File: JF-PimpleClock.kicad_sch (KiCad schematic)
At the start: 59 parts, among them J1 Conn_01x06_Female, J2 Conn_01x02, J3 Conn_01x02, J4 USB_B_Micro, Q1 Q_PMOS_DSG, SW1 SW_Push, SW2 SW_Push, SW3 SW_Push, SW4 SW_Push, U1 ATmega328-P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

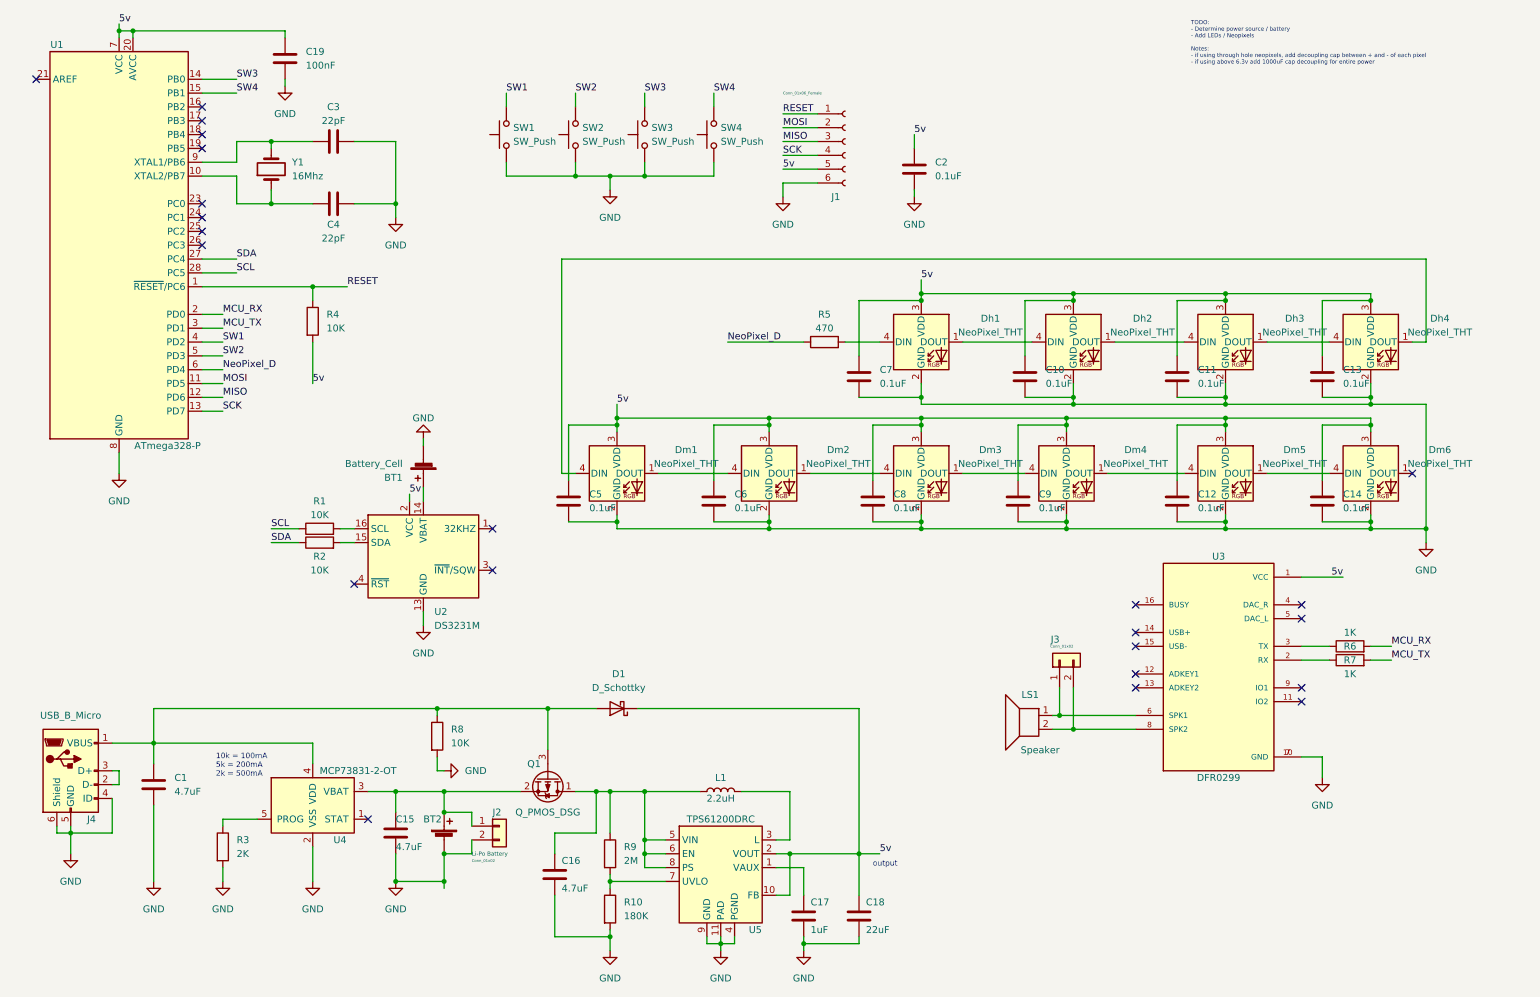
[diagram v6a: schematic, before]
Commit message: revision 2, changed some parts for making it easier to manufacture, fixed the issue with the wrong atmega footprint, added more test points
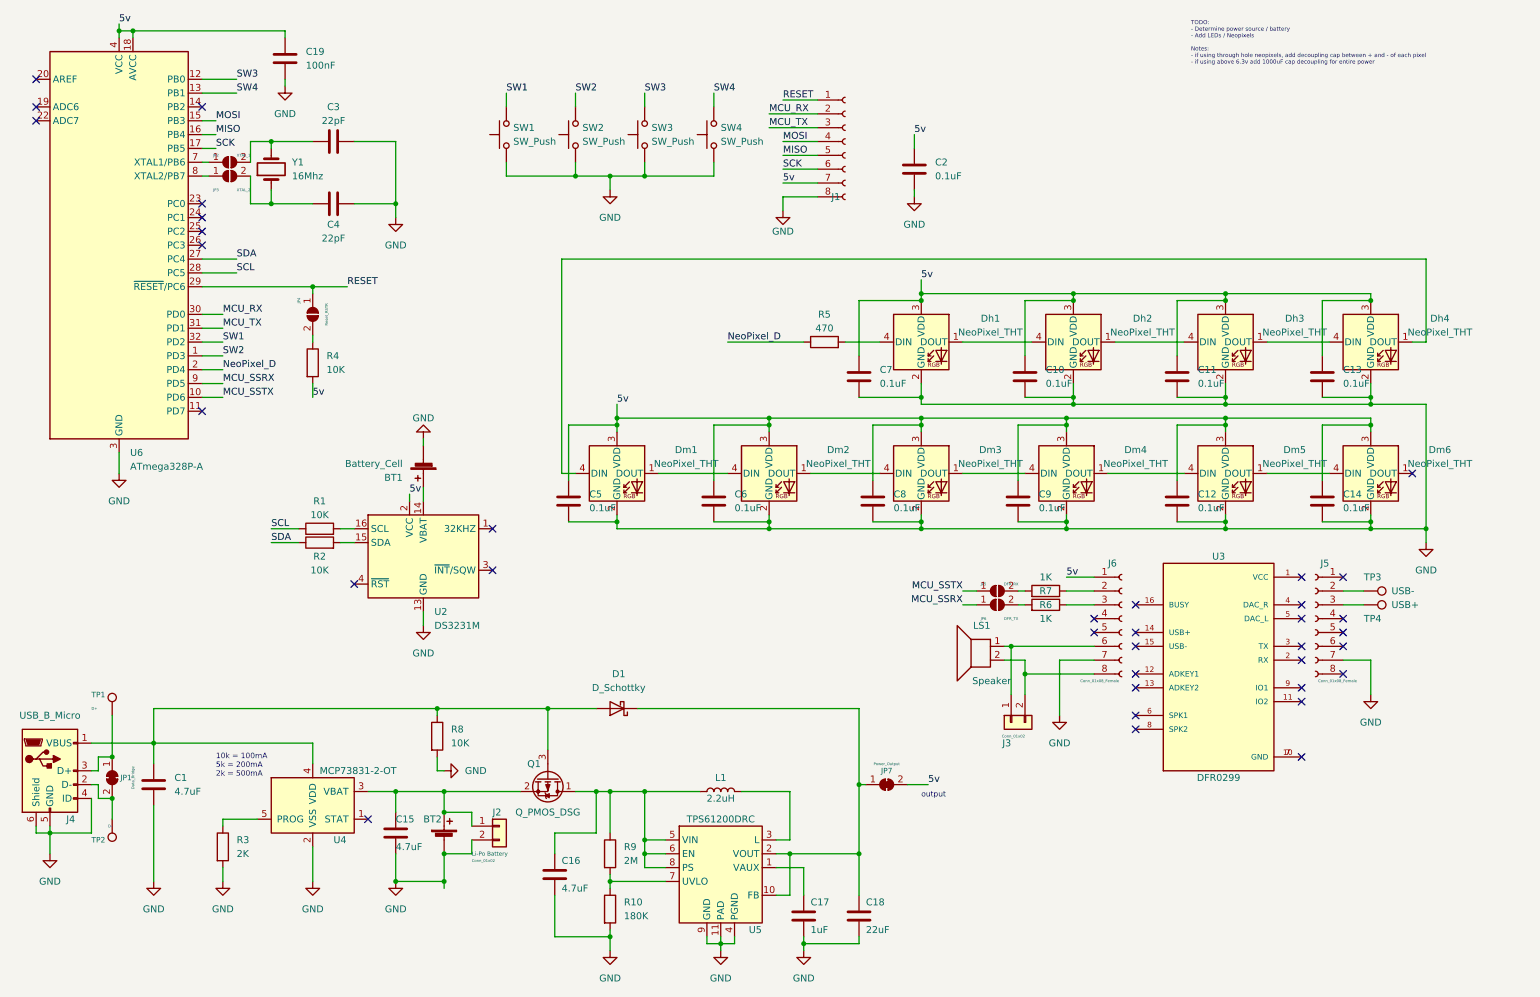
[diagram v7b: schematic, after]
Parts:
- removed U1: ATmega328-P, Package_QFP:TQFP-32_7x7mm_P0.8mm, symbol MCU_Microchip_ATmega:ATmega328-P
- added J5, J6: Conn_01x08_Female, Connector_PinHeader_2.54mm:PinHeader_1x08_P2.54mm_Vertical, symbol Connector:Conn_01x08_Female
- added JP1: Data_Bridge, Jumper:SolderJumper-2_P1.3mm_Bridged_Pad1.0x1.5mm, symbol Jumper:SolderJumper_2_Bridged
- added JP2: XTAL_1, Jumper:SolderJumper-2_P1.3mm_Open_Pad1.0x1.5mm, symbol Jumper:SolderJumper_2_Open
- added JP3: XTAL_2, Jumper:SolderJumper-2_P1.3mm_Open_Pad1.0x1.5mm, symbol Jumper:SolderJumper_2_Open
- added JP4: Reset_RSTR, Jumper:SolderJumper-2_P1.3mm_Open_Pad1.0x1.5mm, symbol Jumper:SolderJumper_2_Open
- added JP5: DFR_RX, Jumper:SolderJumper-2_P1.3mm_Open_Pad1.0x1.5mm, symbol Jumper:SolderJumper_2_Open
- added JP6: DFR_TX, Jumper:SolderJumper-2_P1.3mm_Open_Pad1.0x1.5mm, symbol Jumper:SolderJumper_2_Open
- added JP7: Power_Output, Jumper:SolderJumper-2_P1.3mm_Bridged_Pad1.0x1.5mm, symbol Jumper:SolderJumper_2_Bridged
- added TP1: D+, TestPoint:TestPoint_THTPad_2.5x2.5mm_Drill1.2mm, symbol Connector:TestPoint
- added TP2: D-, TestPoint:TestPoint_THTPad_2.5x2.5mm_Drill1.2mm, symbol Connector:TestPoint
- added TP3: USB-, TestPoint:TestPoint_THTPad_2.5x2.5mm_Drill1.2mm, symbol Connector:TestPoint
- added TP4: USB+, TestPoint:TestPoint_THTPad_2.5x2.5mm_Drill1.2mm, symbol Connector:TestPoint
- added U6: ATmega328P-A, Package_QFP:TQFP-32_7x7mm_P0.8mm, symbol MCU_Microchip_ATmega:ATmega328P-A
- J1: value Conn_01x06_Female -> Conn_01x08_Female; footprint Connector_PinHeader_2.54mm:PinHeader_1x06_P2.54mm_Vertical -> Connector_PinHeader_2.54mm:PinHeader_1x08_P2.54mm_Vertical; symbol Connector:Conn_01x06_Female -> Connector:Conn_01x08_Female
- SW1, SW2, SW3, SW4: footprint Button_Switch_SMD:SW_SPST_B3S-1100 -> Button_Switch_THT:SW_PUSH_6mm_H5mm
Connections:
- net 5v: now also J1.7 (Pin_7), J6.1 (Pin_1), JP7.2 (B), U6.18 (AVCC), U6.4 (VCC), U6.6 (VCC); no longer C18.1, D1.1 (K), J1.5 (Pin_5), U3.1 (VCC), U5.10 (FB), U5.2 (VOUT)
- net GND: now also J1.8 (Pin_8), J5.7 (Pin_7), J6.7 (Pin_7), U6.21 (GND), U6.3 (GND), U6.5 (GND); no longer J1.6 (Pin_6), U3.10 (GND), U3.7 (GND)
- net MCU_RX: now also J1.2 (Pin_2), U6.30 (PD0); no longer R6.2
- net MCU_TX: now also J1.3 (Pin_3), U6.31 (PD1); no longer R7.2
- net MISO: now also J1.5 (Pin_5), U6.16 (PB4); no longer J1.3 (Pin_3)
- net MOSI: now also J1.4 (Pin_4), U6.15 (PB3); no longer J1.2 (Pin_2)
- net NeoPixel_D: now also U6.2 (PD4)
- net RESET: now also JP4.1 (A), U6.29 (~{RESET}/PC6); no longer R4.1
- net SCK: now also J1.6 (Pin_6), U6.17 (PB5); no longer J1.4 (Pin_4)
- net SCL: now also U6.28 (PC5)
- net SDA: now also U6.27 (PC4)
- net SW1: now also U6.32 (PD2)
- net SW2: now also U6.1 (PD3)
- net SW3: now also U6.12 (PB0)
- net SW4: now also U6.13 (PB1)
- net at J3.1 (Pin_1), LS1.1: now also J6.6 (Pin_6); no longer U3.6 (SPK1)
- net at J3.2 (Pin_2), LS1.2: now also J6.8 (Pin_8); no longer U3.8 (SPK2)
- net at J4.3 (D+): now also JP1.1 (A), TP1.1; no longer J4.2 (D-)
- net at R6.1: now also J6.3 (Pin_3); no longer U3.3 (TX)
- net at C4.1, Y1.1: now also JP3.2 (B)
- net at C3.1, Y1.2: now also JP2.2 (B)
- net at R7.1: now also J6.2 (Pin_2); no longer U3.2 (RX)
- new net: C18.1, D1.1 (K), JP7.1 (A), U5.10 (FB), U5.2 (VOUT)
- new net: J4.2 (D-), JP1.2 (B), TP2.1
- new net: JP6.2 (B), R6.2
- new net: JP5.2 (B), R7.2
- new net: JP4.2 (B), R4.1
- new net: J5.2 (Pin_2), TP3.1
- new net: J5.3 (Pin_3), TP4.1
- new net: JP2.1 (A), U6.7 (XTAL1/PB6)
- new net: JP3.1 (A), U6.8 (XTAL2/PB7)
- new net: U3.10 (GND), U3.7 (GND)
- new net MCU_SSRX: JP6.1 (A), U6.9 (PD5)
- new net MCU_SSTX: JP5.1 (A), U6.10 (PD6)
- no-connect marks 23 -> 36
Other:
- moved on the sheet: J3, J4, LS1, R4, R6, R7

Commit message: update from projects
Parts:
- removed JP4: Reset_RSTR, Jumper:SolderJumper-2_P1.3mm_Open_Pad1.0x1.5mm, symbol Jumper:SolderJumper_2_Open
- removed JP5: DFR_RX, Jumper:SolderJumper-2_P1.3mm_Open_Pad1.0x1.5mm, symbol Jumper:SolderJumper_2_Open
- removed JP6: DFR_TX, Jumper:SolderJumper-2_P1.3mm_Open_Pad1.0x1.5mm, symbol Jumper:SolderJumper_2_Open
- removed JP7: Power_Output, Jumper:SolderJumper-2_P1.3mm_Bridged_Pad1.0x1.5mm, symbol Jumper:SolderJumper_2_Bridged
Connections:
- net 5v: now also C18.1, D1.1 (K), U5.10 (FB), U5.2 (VOUT)
- net MCU_SSRX: now also R6.2
- net MCU_SSTX: now also R7.2
- net RESET: now also R4.1
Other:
- note added: "TODO: - Change dimmer to knob/slider that is also the power, bonus is a slider that triggers a pitchslide sound - Audio tester button, if pressed twice increments to next set sound in list - fix debounce to be more responsive, if we cant fix it then change buttons - Add LEDs / Neopixels - new switch for swapping reading direction, with indicator - blue wire mistake! Bonus: - test circuit of capac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"
- note removed: "TODO: - Determine power source / battery - Add LEDs / Neopixels Notes: - if using through hole neopixels, add decoupling cap between + and - of each pixel - if using above 6.3v add 1000uF cap decoupling for entire power"
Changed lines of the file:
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@@
     (title "JoeyFrank - Pimple Clock Circuit")
     (date "2022-12-23")
-    (rev "2")
+    (rev "3")
     (company "DCR")
   )
@@
   (no_connect (at 250.19 138.43))
   (no_connect (at 250.19 123.19))
-  (wire (pts (xy 187.96 120.65) (xy 190.5 120.65))
-    (stroke (width 0) (type default) (color 0 0 0 0))
-  )
   (wire (pts (xy 147.32 157.48) (xy 156.21 157.48))
     (stroke (width 0) (type default) (color 0 0 0 0))
@@
     (stroke (width 0) (type default) (color 0 0 0 0))
   )
-  (wire (pts (xy 198.12 123.19) (xy 199.39 123.19))
-    (stroke (width 0) (type default) (color 0 0 0 0))
-  )
   (wire (pts (xy 33.02 16.51) (xy 33.02 17.78))
     (stroke (width 0) (type default) (color 0 0 0 0))
@@
     (stroke (width 0) (type default) (color 0 0 0 0))
   )
-  (wire (pts (xy 198.12 120.65) (xy 199.39 120.65))
+  (wire (pts (xy 187.96 120.65) (xy 199.39 120.65))
     (stroke (width 0) (type default) (color 0 0 0 0))
   )
@@
     (stroke (width 0) (type default) (color 0 0 0 0))
   )
-  (wire (pts (xy 168.91 156.21) (xy 170.18 156.21))
+  (wire (pts (xy 168.91 156.21) (xy 181.61 156.21))
     (stroke (width 0) (type default) (color 0 0 0 0))
   )
@@
     (stroke (width 0) (type default) (color 0 0 0 0))
   )
-  (wire (pts (xy 68.58 64.77) (xy 68.58 66.04))
-    (stroke (width 0) (type default) (color 0 0 0 0))
-  )
   (wire (pts (xy 153.67 176.53) (xy 156.21 176.53))
     (stroke (width 0) (type default) (color 0 0 0 0))
@@
     (stroke (width 0) (type default) (color 0 0 0 0))
   )
-  (wire (pts (xy 187.96 123.19) (xy 190.5 123.19))
+  (wire (pts (xy 187.96 123.19) (xy 199.39 123.19))
     (stroke (width 0) (type default) (color 0 0 0 0))
   )
@@
     (stroke (width 0) (type default) (color 0 0 0 0))
   )
-  (wire (pts (xy 177.8 156.21) (xy 181.61 156.21))
-    (stroke (width 0) (type default) (color 0 0 0 0))
-  )
   (wire (pts (xy 113.03 176.53) (xy 113.03 184.15))
     (stroke (width 0) (type default) (color 0 0 0 0))
@@
     (stroke (width 0) (type default) (color 0 0 0 0))
   )
-  (wire (pts (xy 68.58 73.66) (xy 68.58 74.93))
+  (wire (pts (xy 68.58 64.77) (xy 68.58 74.93))
     (stroke (width 0) (type default) (color 0 0 0 0))
   )
@@
     (effects (font (size 1 1)) (justify left bottom))
   )
-  (text "TODO: \n- Determine power source / battery\n- Add LEDs / Neopixels\n\nNotes:\n- if using through hole neopixels, add decoupling cap between + and - of each pixel\n- if using above 6.3v add 1000uF cap decoupling for entire power"
-    (at 229.87 24.13 0)
+  (text "TODO: \n- Change dimmer to knob/slider that is also the power, bonus is a slider that triggers a pitchslide sound\n- Audio tester button, if pressed twice increments to next set sound in list\n- fix debounce to be more responsive, if we cant fix it then change buttons\n- Add LEDs / Neopixels\n- new switch for swapping reading direction, with indicator \n- blue wire mistake!\n\nBonus: \n- test circuit of capacitive touch slider\n- test circuit of diffuse colo grid board\n\nNotes:\n- if using through hole neopixels, add decoupling cap between + and - of each pixel\n- if using above 6.3v add 1000uF cap decoupling for entire power"
+    (at 213.36 35.56 0)
     (effects (font (size 0.75 0.75)) (justify left bottom))
   )
@@
     )
     (property "Datasheet" "~" (id 3) (at 196.85 144.78 0)
-      (effects (font (size 1.27 1.27)) hide)
-    )
-    (pin "1")
-    (pin "2")
-  )
-  (symbol (lib_id "Jumper:SolderJumper_2_Bridged") (at 173.99 156.21 0) (unit 1)
-    (in_bom yes) (on_board yes)
-    (property "Reference" "JP7" (id 0) (at 173.99 153.67 0)
-      (effects (font (size 1 1)))
-    )
-    (property "Value" "Power_Output" (id 1) (at 173.99 152.4 0)
-      (effects (font (size 0.5 0.5)))
-    )
-    (property "Footprint" "Jumper:SolderJumper-2_P1.3mm_Bridged_Pad1.0x1.5mm" (id 2) (at 173.99 156.21 0)
-      (effects (font (size 1.27 1.27)) hide)
-    )
-    (property "Datasheet" "~" (id 3) (at 173.99 156.21 0)
       (effects (font (size 1.27 1.27)) hide)
     )
@@
     (pin "8")
   )
-  (symbol (lib_id "Jumper:SolderJumper_2_Open") (at 194.31 123.19 0) (unit 1)
-    (in_bom yes) (on_board yes)
-    (property "Reference" "JP6" (id 0) (at 191.77 125.73 0)
-      (effects (font (size 0.5 0.5)))
-    )
-    (property "Value" "DFR_TX" (id 1) (at 196.85 125.73 0)
-      (effects (font (size 0.5 0.5)))
-    )
-    (property "Footprint" "Jumper:SolderJumper-2_P1.3mm_Open_Pad1.0x1.5mm" (id 2) (at 194.31 123.19 0)
-      (effects (font (size 0.5 0.5)) hide)
-    )
-    (property "Datasheet" "~" (id 3) (at 194.31 123.19 0)
-      (effects (font (size 0.5 0.5)) hide)
-    )
-    (pin "1")
-    (pin "2")
-  )
   (symbol (lib_id "Device:R") (at 203.2 120.65 270) (mirror x) (unit 1)
     (in_bom yes) (on_board yes)
@@
     )
     (pin "1")
-  )
-  (symbol (lib_id "Jumper:SolderJumper_2_Open") (at 68.58 69.85 270) (unit 1)
-    (in_bom yes) (on_board yes)
-    (property "Reference" "JP4" (id 0) (at 66.04 67.31 0)
-      (effects (font (size 0.5 0.5)))
-    )
-    (property "Value" "Reset_RSTR" (id 1) (at 71.12 69.85 0)
-      (effects (font (size 0.5 0.5)))
-    )
-    (property "Footprint" "Jumper:SolderJumper-2_P1.3mm_Open_Pad1.0x1.5mm" (id 2) (at 68.58 69.85 0)
-      (effects (font (size 0.5 0.5)) hide)
-    )
-    (property "Datasheet" "~" (id 3) (at 68.58 69.85 0)
-      (effects (font (size 0.5 0.5)) hide)
-    )
-    (pin "1")
-    (pin "2")
   )
   (symbol (lib_id "Device:R") (at 69.85 111.76 90) (unit 1)
@@
     (pin "2")
   )
-  (symbol (lib_id "Jumper:SolderJumper_2_Open") (at 194.31 120.65 0) (unit 1)
-    (in_bom yes) (on_board yes)
-    (property "Reference" "JP5" (id 0) (at 191.77 119.38 0)
-      (effects (font (size 0.5 0.5)))
-    )
-    (property "Value" "DFR_RX" (id 1) (at 196.85 119.38 0)
-      (effects (font (size 0.5 0.5)))
-    )
-    (property "Footprint" "Jumper:SolderJumper-2_P1.3mm_Open_Pad1.0x1.5mm" (id 2) (at 194.31 120.65 0)
-      (effects (font (size 0.5 0.5)) hide)
-    )
-    (property "Datasheet" "~" (id 3) (at 194.31 120.65 0)
-      (effects (font (size 0.5 0.5)) hide)
-    )
-    (pin "1")
-    (pin "2")
-  )
   (symbol (lib_id "Jumper:SolderJumper_2_Open") (at 53.34 41.91 0) (unit 1)
     (in_bom yes) (on_board yes)
@@
       (reference "JP3") (unit 1) (value "XTAL_2") (footprint "Jumper:SolderJumper-2_P1.3mm_Open_Pad1.0x1.5mm")
     )
-    (path "/5be361a1-1c92-4495-ac0a-7428d78836b8"
-      (reference "JP4") (unit 1) (value "Reset_RSTR") (footprint "Jumper:SolderJumper-2_P1.3mm_Open_Pad1.0x1.5mm")
-    )
-    (path "/aeb54517-f47e-4fc1-ac39-543e769bc52c"
-      (reference "JP5") (unit 1) (value "DFR_RX") (footprint "Jumper:SolderJumper-2_P1.3mm_Open_Pad1.0x1.5mm")
-    )
-    (path "/4c6b490d-28f7-4003-bc5a-7cdea0c43b42"
-      (reference "JP6") (unit 1) (value "DFR_TX") (footprint "Jumper:SolderJumper-2_P1.3mm_Open_Pad1.0x1.5mm")
-    )
-    (path "/070807d0-8b9f-4bbe-9668-2dd302d986b0"
-      (reference "JP7") (unit 1) (value "Power_Output") (footprint "Jumper:SolderJumper-2_P1.3mm_Bridged_Pad1.0x1.5mm")
-    )
     (path "/6b052e76-7c7c-4320-91eb-7f32dcd4f73e"
